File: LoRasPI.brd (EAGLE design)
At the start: 37.8 x 17.9 mm, 12 parts, among them J1 JUMPER_1X30805

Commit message: Bump to V1.1
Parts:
- removed U$1: (no value), _c2h:LOGO_CH2I_75MM
- added D0: 1N4148, Seeed-Discrete:SOD123-2.7X1.6
- added D3: TX/RX, _c2h:0805-LED-LARGEPADS
- added D4: CS, _c2h:0805-LED-LARGEPADS
- added R3: 10K, _c2h:0805-RES
- D1: value TX/RX -> 1N4148; device _c2h:0805-LED-LARGEPADS -> Seeed-Discrete:SOD123-2.7X1.6
- D2: value CS -> 1N4148; device _c2h:0805-LED-LARGEPADS -> Seeed-Discrete:SOD123-2.7X1.6
- moved R1 31.5 mm to (37.1, 10.2), flipped to the bottom, turned to 0 degrees
- moved D1 18.0 mm to (24.1, 21.6), flipped to the bottom, turned to 0 degrees
- moved D2 12.8 mm to (24.1, 23.5), flipped to the bottom, turned to 0 degrees
- moved C1 2.75 mm to (24.5, 16.4), turned to 90 degrees
- moved C2 2.50 mm to (27.6, 16.4), turned to 90 degrees
- moved U$4 1.45 mm to (19.0, 14.0)
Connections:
- new net CS: HOPE-RF.NSS, J1.2, R2.2
- new net DIO0: D0.1, HOPE-RF.DIO0
- new net DIO1: D1.1, HOPE-RF.DIO1
- new net DIO2: D2.1, HOPE-RF.DIO2
- net 3V3: now also R3.1
- net CE0: no longer HOPE-RF.NSS, J1.2, R2.2
- net GND: now also D3.MINUS, D4.MINUS; no longer D1.MINUS, D2.MINUS
- net GPIO25: now also D0.2, D1.2, D2.2, R3.2; no longer HOPE-RF.DIO0
- net N$1: now also D3.PLUS; no longer D1.PLUS
- net N$2: now also D4.PLUS; no longer D2.PLUS
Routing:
- net GPIO23: track 3.12 -> 33.8 mm
- net CE0: track 44.6 -> 14.0 mm, vias 1 -> 0
- net CS: track 0.00 -> 29.9 mm, vias 0 -> 1
- net N$1: track 29.5 -> 2.19 mm, vias 0 -> 1
- net GPIO22: track 18.6 -> 8.07 mm, vias 0 -> 1
- net GND: track 0.00 -> 6.72 mm, vias 24 -> 50
- net 3V3: track 28.5 -> 33.7 mm
- net DIO0: track 0.00 -> 3.01 mm, vias 0 -> 1
- net DIO1: track 0.00 -> 3.00 mm, vias 0 -> 1
- net DIO2: track 0.00 -> 3.00 mm, vias 0 -> 1
- net GPIO25: track 28.7 -> 28.4 mm, vias 1 -> 0
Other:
- board size 37.8 x 17.9 mm -> 37.8 x 16 mm
- board text added: "CS"
- board text added: "LoRasPI V1.1"
- board text added: "RFM69HCW"
- board text added: "RFM92/95"
- board text added: "RFM96/98"
- board text removed: "CS of RFM9x Lora Module"
- board text removed: "LoRasPI V1.0"
- board text removed: "LoRasPI V1.0 http://hallard.me"

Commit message: Version 1.2
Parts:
- D4: value CS -> LED
- moved R3 0.25 mm to (18.7, 21.6), turned to 270 degrees
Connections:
- net 3V3: no longer R3.1
- net CS: no longer J1.2, R2.2
- net GND: now also R3.1
- net GPIO24: now also R2.2; no longer HOPE-RF.DIO5
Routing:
- net GPIO24: track 9.31 -> 31.6 mm, vias 0 -> 1
- net CS: track 29.9 -> 8.18 mm
- net 3V3: track 33.7 -> 25.9 mm
- net GPIO25: track 28.4 -> 26.1 mm
- net GND: track 6.72 -> 7.25 mm
- net GPIO22: vias 1 -> 0
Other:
- board text added: "LoRasPI V1.2"
- board text removed: "LoRasPI V1.1"

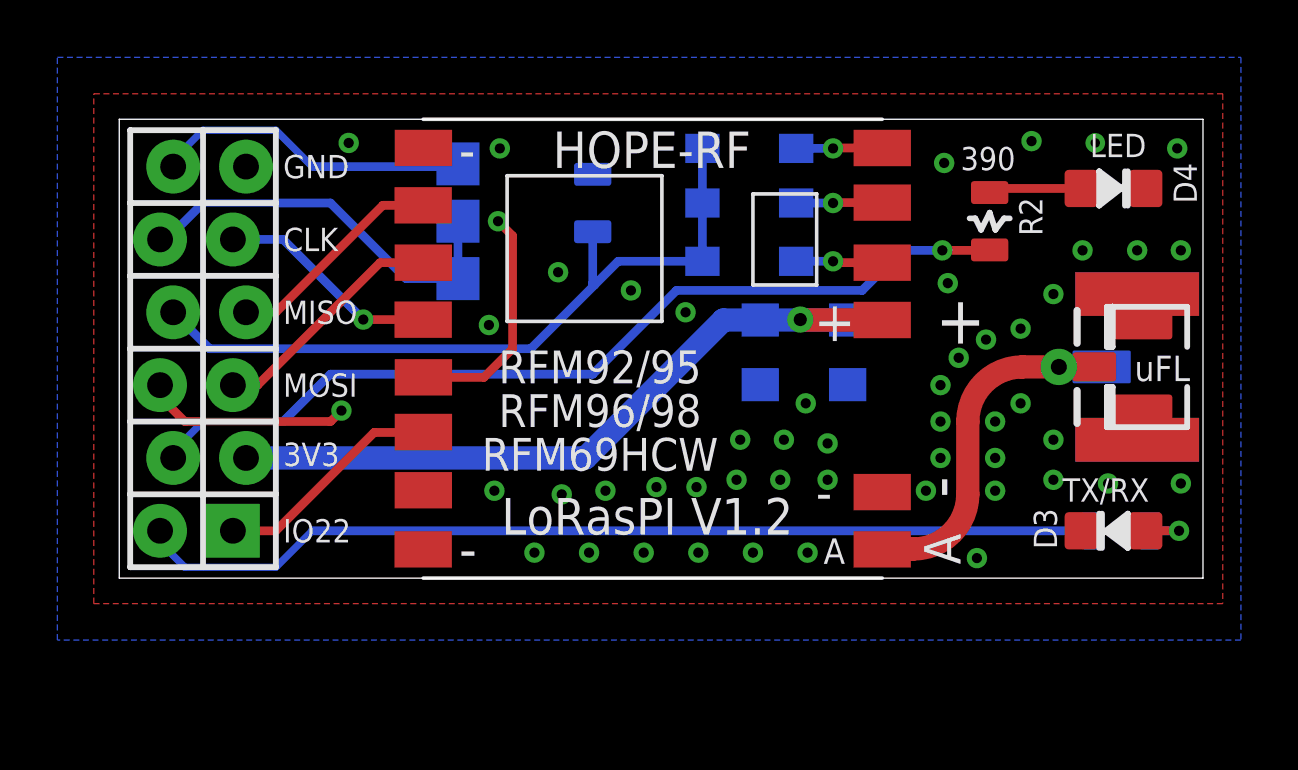
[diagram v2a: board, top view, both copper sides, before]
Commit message: V1.2a, fixed missing trace
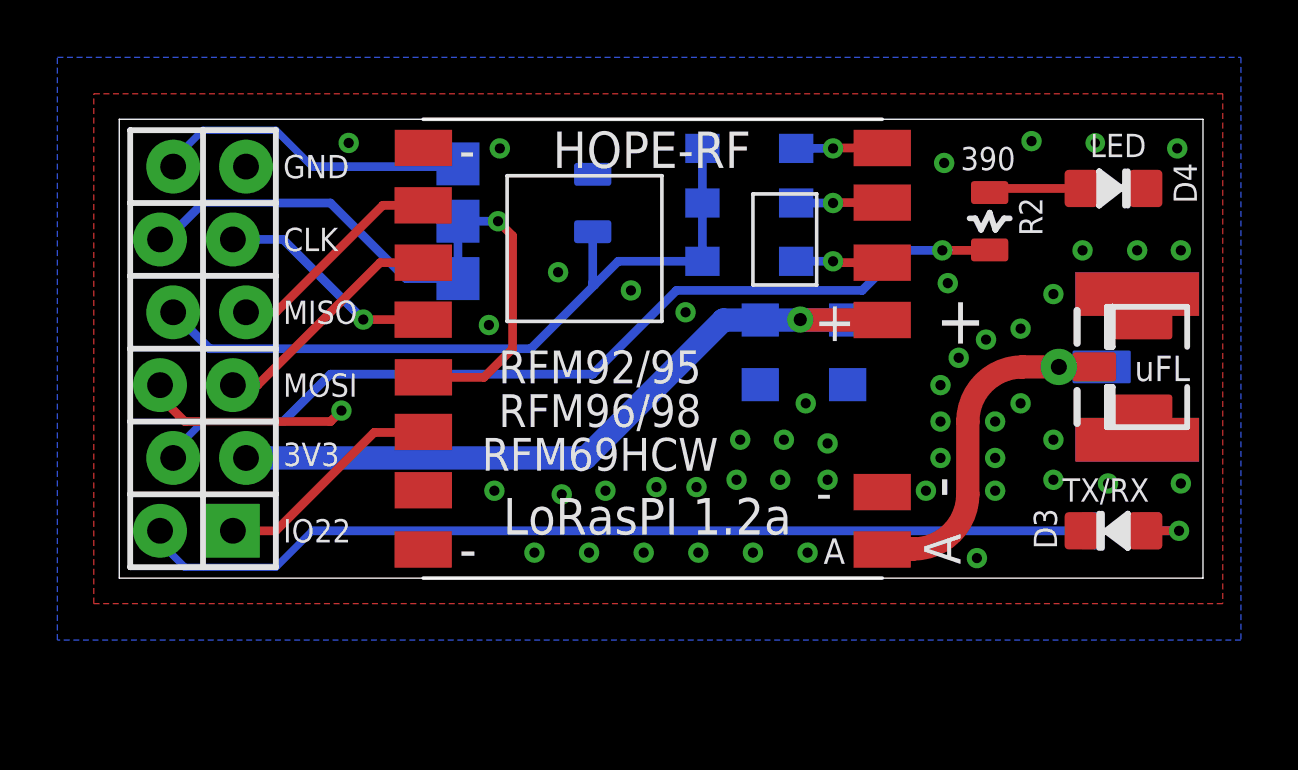
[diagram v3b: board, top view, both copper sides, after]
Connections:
- net CS: now also J1.2
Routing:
- net CS: track 8.18 -> 9.58 mm
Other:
- board text added: "LoRasPI 1.2a"
- board text removed: "LoRasPI V1.2"
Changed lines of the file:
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@@
 <wire x1="39.951" y1="24.511" x2="2.159" y2="24.511" width="0" layer="20"/>
 <wire x1="2.159" y1="24.511" x2="2.159" y2="8.509" width="0" layer="20"/>
-<text x="20.574" y="10.668" size="1.27" layer="21" font="vector" ratio="15" align="center">LoRasPI V1.2</text>
+<text x="20.574" y="10.668" size="1.27" layer="21" font="vector" ratio="15" align="center">LoRasPI 1.2a</text>
 <text x="7.874" y="10.16" size="0.8128" layer="21" font="vector" ratio="15" align="center-left">IO22</text>
 <text x="7.874" y="12.827" size="0.8128" layer="21" font="vector" ratio="15" align="center-left">3V3</text>
@@
 <text x="7.874" y="20.32" size="0.8128" layer="21" font="vector" ratio="15" align="center-left">CLK</text>
 <text x="7.874" y="22.86" size="0.8128" layer="21" font="vector" ratio="15" align="center-left">GND</text>
-<text x="20.828" y="10.414" size="1.27" layer="22" font="vector" ratio="15" rot="MR0" align="center">LoRasPI V1.2</text>
+<text x="20.828" y="10.414" size="1.27" layer="22" font="vector" ratio="15" rot="MR0" align="center">LoRasPI 1.2a</text>
 <text x="11.557" y="20.955" size="1.016" layer="22" font="vector" ratio="15" rot="MR0" align="center">CS</text>
 <text x="30.861" y="9.525" size="1.27" layer="21" font="vector" ratio="15" rot="R90" align="center">A</text>
@@
 <via x="15.367" y="20.955" extent="1-16" drill="0.3556" diameter="0.7112"/>
 <wire x1="12.7645" y1="15.51" x2="14.875" y2="15.51" width="0.3048" layer="1"/>
+<contactref element="J1" pad="2"/>
+<wire x1="15.367" y1="20.955" x2="13.97" y2="20.955" width="0.3048" layer="16"/>
 </signal>
 </signals>
